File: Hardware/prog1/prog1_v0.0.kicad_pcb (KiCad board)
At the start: 2 copper layers, 16 x 25 mm, 6 parts, among them J1 Conn_01x02, SW1 SW_Push

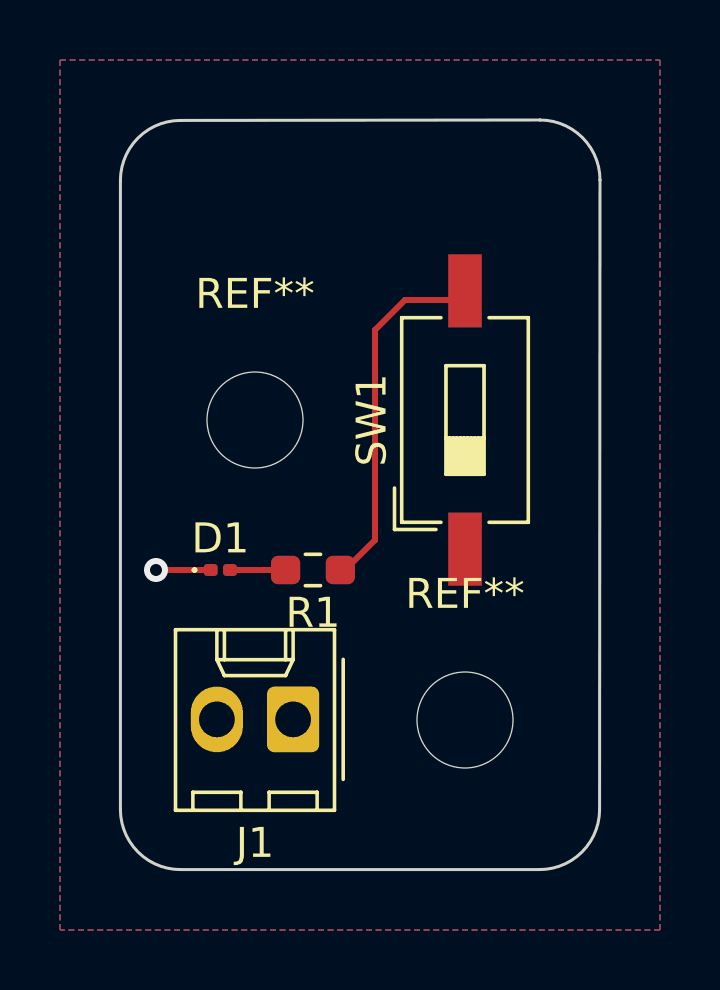
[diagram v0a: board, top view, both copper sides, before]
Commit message: edit LED footprint
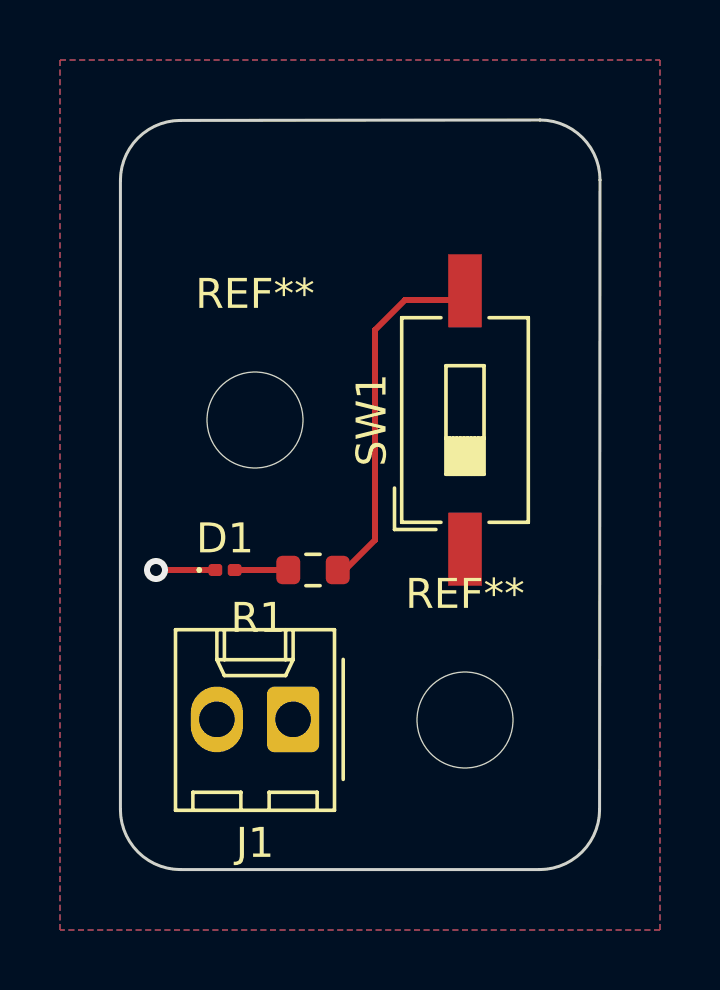
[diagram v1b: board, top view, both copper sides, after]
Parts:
- R1: footprint Resistor_SMD:R_0603_1608Metric_Pad0.98x0.95mm_HandSolder -> Resistor_SMD:R_0603_1608Metric
- moved D1 0.16 mm to (25.5, 32.0)
